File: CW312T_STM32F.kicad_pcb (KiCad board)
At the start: 2 copper layers, 58.7 x 53.7 mm, 25 parts, among them J1 HDR_6_2.54, P1 PCIEx4 EDGE CONNECTOR, U1 STM32F100RBT6B

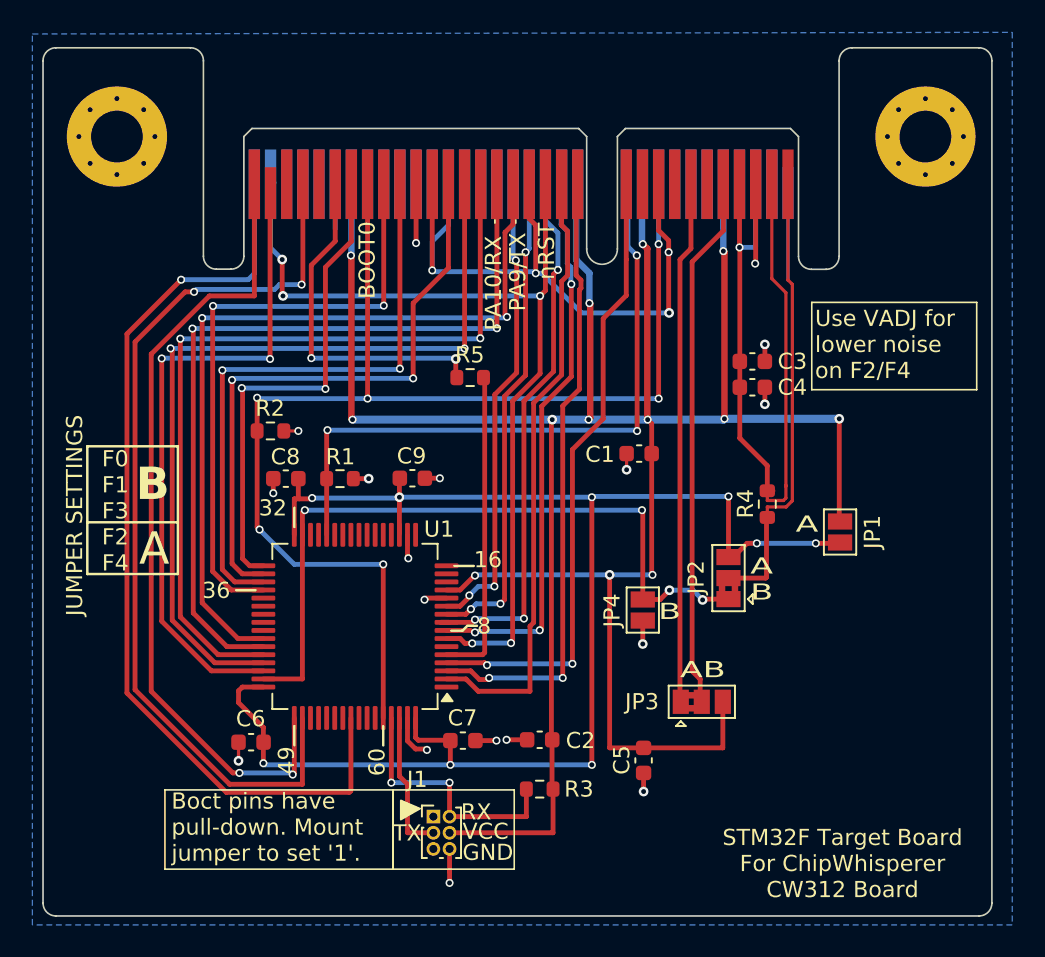
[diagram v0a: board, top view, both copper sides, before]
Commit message: updated schematic and pcb after library reorganization, and updated pin header to include proper footprint
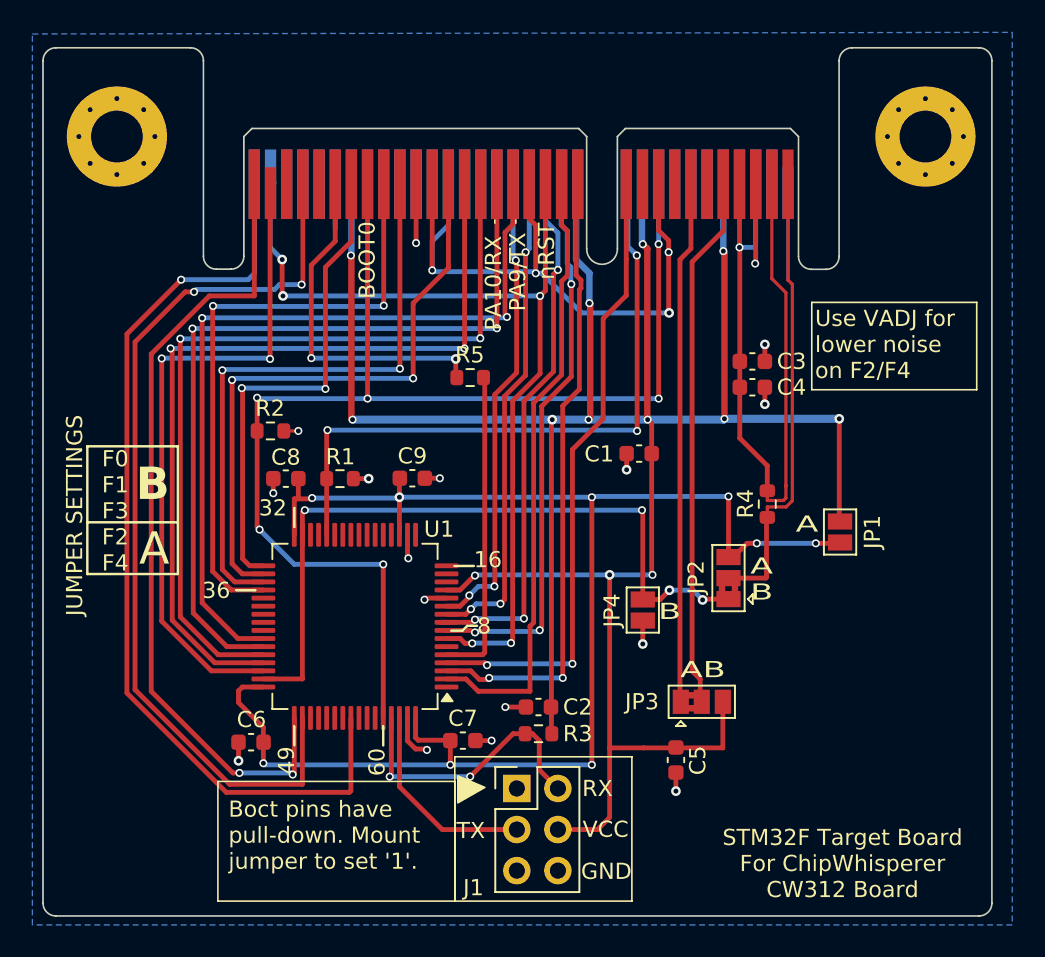
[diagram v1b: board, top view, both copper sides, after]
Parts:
- C1, C2, C4, C5, C6, C7, C8, C9: value CAP_100n_50V_0603 -> CAP_100n_25V_0603
- C3: value CAP_2u2_16V_0603 -> CAP_2u2_10V_0603
- J1: value HDR_6_2.54 -> HDR_2x3_2.54; footprint Connector_PinHeader_1.00mm:PinHeader_2x03_P1.00mm_Vertical -> Connector_PinHeader_2.54mm:PinHeader_2x03_P2.54mm_Vertical
- R1, R2, R3: value 10K -> RES_10k_0603
- R5: value 51R_0603 -> RES_22R_0603
- moved J1 5.45 mm to (140.6, 101.4)
- moved R3 3.43 mm to (141.9, 98.0)
- moved C2 2.03 mm to (141.9, 96.3), turned to 0 degrees
- moved C5 2.00 mm to (150.4, 99.6), turned to 90 degrees
- turned C1 to 0 degrees
- turned C3 to 180 degrees
- turned C4 to 180 degrees
- turned C6 to 0 degrees
- turned C7 to 180 degrees
- turned C8 to 0 degrees
- turned C9 to 180 degrees
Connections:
- C1 pad 1: VCC -> GND
- C1 pad 2: GND -> VCC
- C2 pad 1: VCC -> GND
- C2 pad 2: GND -> VCC
- C3 pad 1: /FILT_HP -> GND
- C3 pad 2: GND -> /FILT_HP
- C4 pad 1: /FILT_HP -> GND
- C4 pad 2: GND -> /FILT_HP
- C5 pad 1: VCC -> GND
- C5 pad 2: GND -> VCC
- C6 pad 1: Net-(U1B-VDD_1) -> GND
- C6 pad 2: GND -> Net-(U1B-VDD_1)
- C7 pad 1: Net-(U1B-VDD_1) -> GND
- C7 pad 2: GND -> Net-(U1B-VDD_1)
- C8 pad 1: Net-(U1B-VDD_1) -> GND
- C8 pad 2: GND -> Net-(U1B-VDD_1)
- C9 pad 1: Net-(U1B-VDD_1) -> GND
- C9 pad 2: GND -> Net-(U1B-VDD_1)
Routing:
- net VCC: track 171.1 -> 166.2 mm
- net /CAN TX: track 8.91 -> 12.6 mm
- net GND: track 78.5 -> 76.1 mm, vias 22 -> 21
- net /CAN RX: track 16.1 -> 17.7 mm
